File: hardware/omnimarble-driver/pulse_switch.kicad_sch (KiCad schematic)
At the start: 33 parts, among them J3 E-STOP-NC, J4 ARM-KEY, Q10 SFT040N150C3, Q11 SFT040N150C3, Q12 SFT040N150C3, U6 74LVC1G08, U7 UCC27524A, U8 UCC27524A

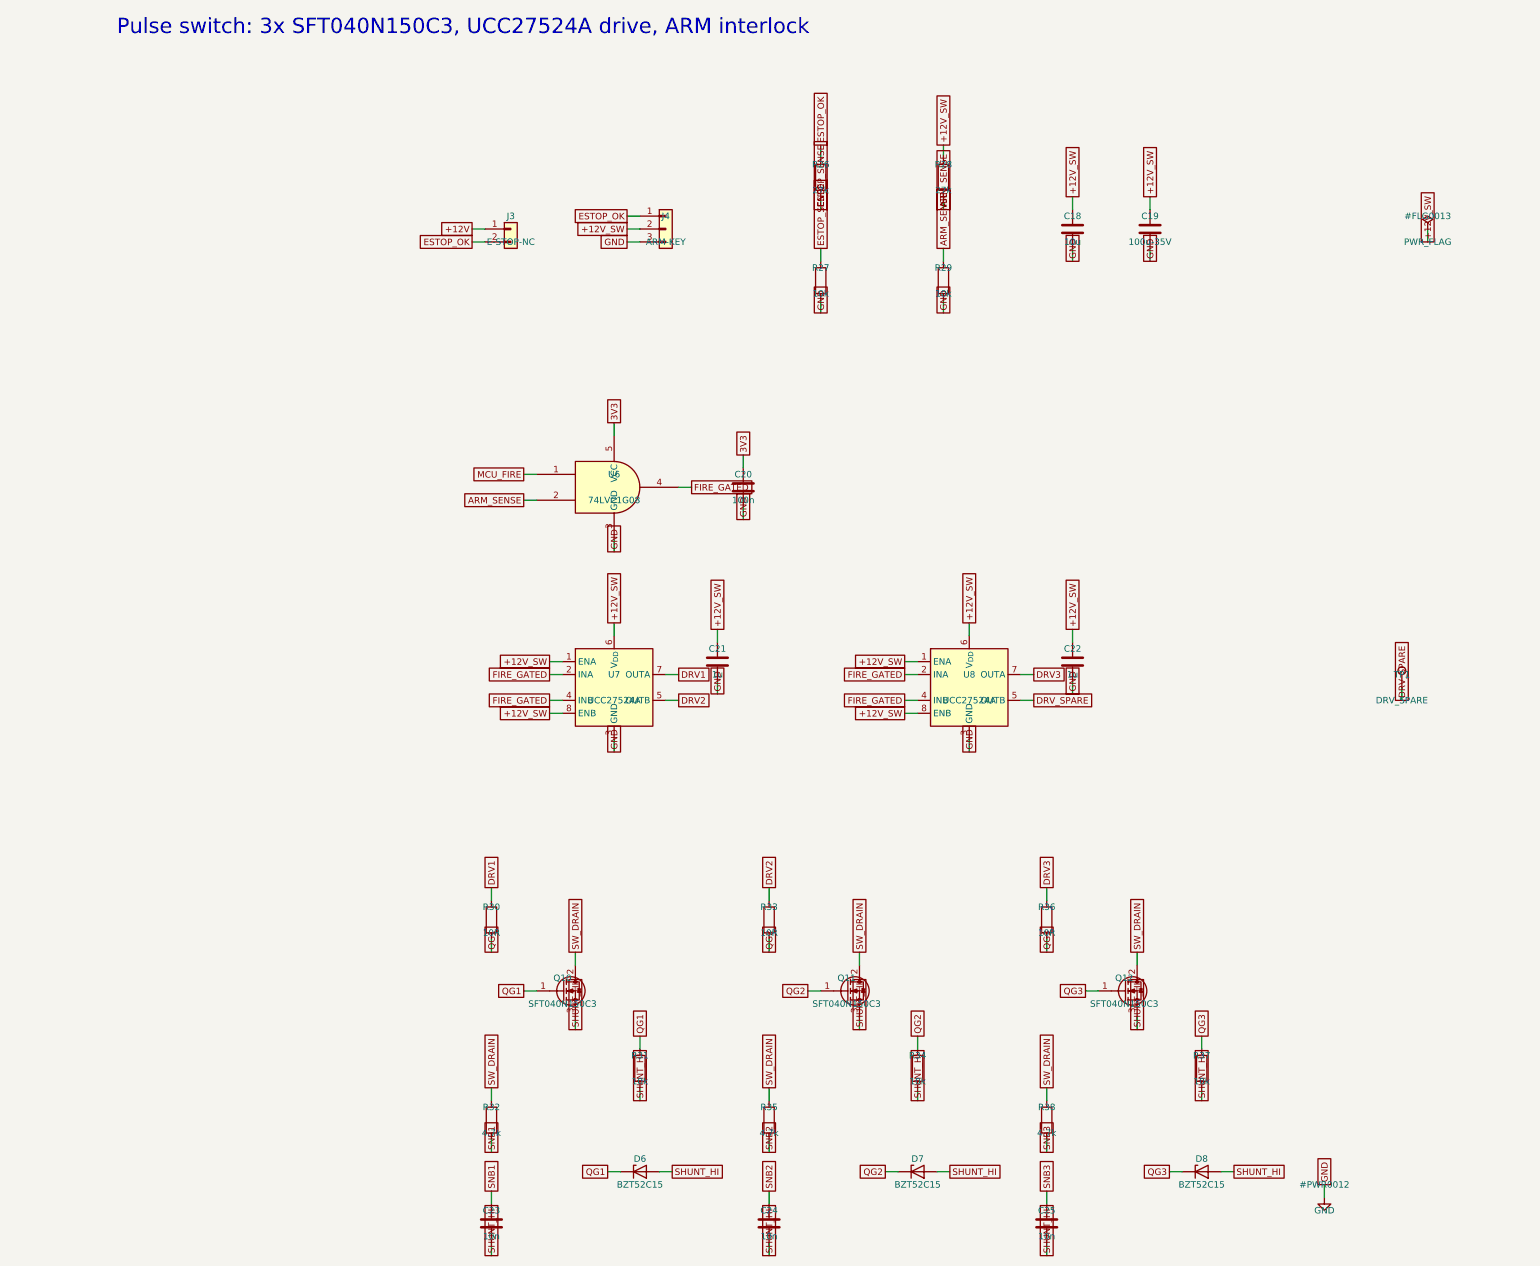
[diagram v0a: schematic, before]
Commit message: Address external design review: boost FB + OVP redesign, BOM freeze
Review findings accepted and fixed (each verified by machine check):

1. Boost feedback network was wrong (confirmed: as-drawn spanned
   54-68V with PWM inverted vs the comment). Redesigned: RT/RB/RJ =
   100k/10k/9.1k with the exact transfer function documented in the
   schematic and design-calcs.md. PWM=0 (MCU-dead state) commands
   55.0V; full PWM commands 18.7V (below the 24.5V converter floor).
   New calcs.py asserts both endpoints.
2. OVP tripped at 55.6V, not the claimed 63V (confirmed). Redesigned:
   CJ431 (+/-0.5%) + 100k/4.3k 1% -> 60.5V nominal, 59.1-62.0V across
   tolerances. Protection ladder asserted in calcs.py: 55V operating
   < 59.1V trip-min, 62.0V trip-max < 63V cap rating - 1V. Operating
   ceiling deliberately reduced 60->55V to keep the bands disjoint.
3. BOM/schematic controller split-brain: bom.csv was stale
   (pre-UC3843 swap); regenerated from parts.py. Both now UC3843B.
4. High-power placeholders now real orderable parts (LCSC-verified):
   47R/5W SQM cement C5807995, dump redesigned to 2x 100R/10W cement
   in series C216413 (no 20-25W part stocked on LCSC; 5.3s to <5V),
   50mR/3W 2512 C2994645, 63V/35V electrolytics C28241/C176666, 10uH
   Sunlord C79272, MINI fuses+Keystone 3568 holders, buzzer, Pico
   sockets/breakout headers. Single documented exception: the 6.8k/2W
   bleed (CRH2512J6K80E04Z) is marked ORDER-REVIEW because LCSC's
   search is uncrawlable - validate.py allowlists it visibly.
5. validate.py pulled forward from the fab phase: fails on unknown
   footprints, blank LCSC on machine-placed parts, missing Variant
   fields, and duplicate refs; generates per-variant gate-rail BOMs
   (bom_rail_emit/recv.csv). Caught two bad footprint names.
6. Paralleling constraints now on the schematic (same-lot FETs,
   symmetric copper, <25mm gate loops, driver return at shunt star).
7. Fail-safe defaults hardened: MCU_FIRE and FIRE_GATED get explicit
   pulldow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
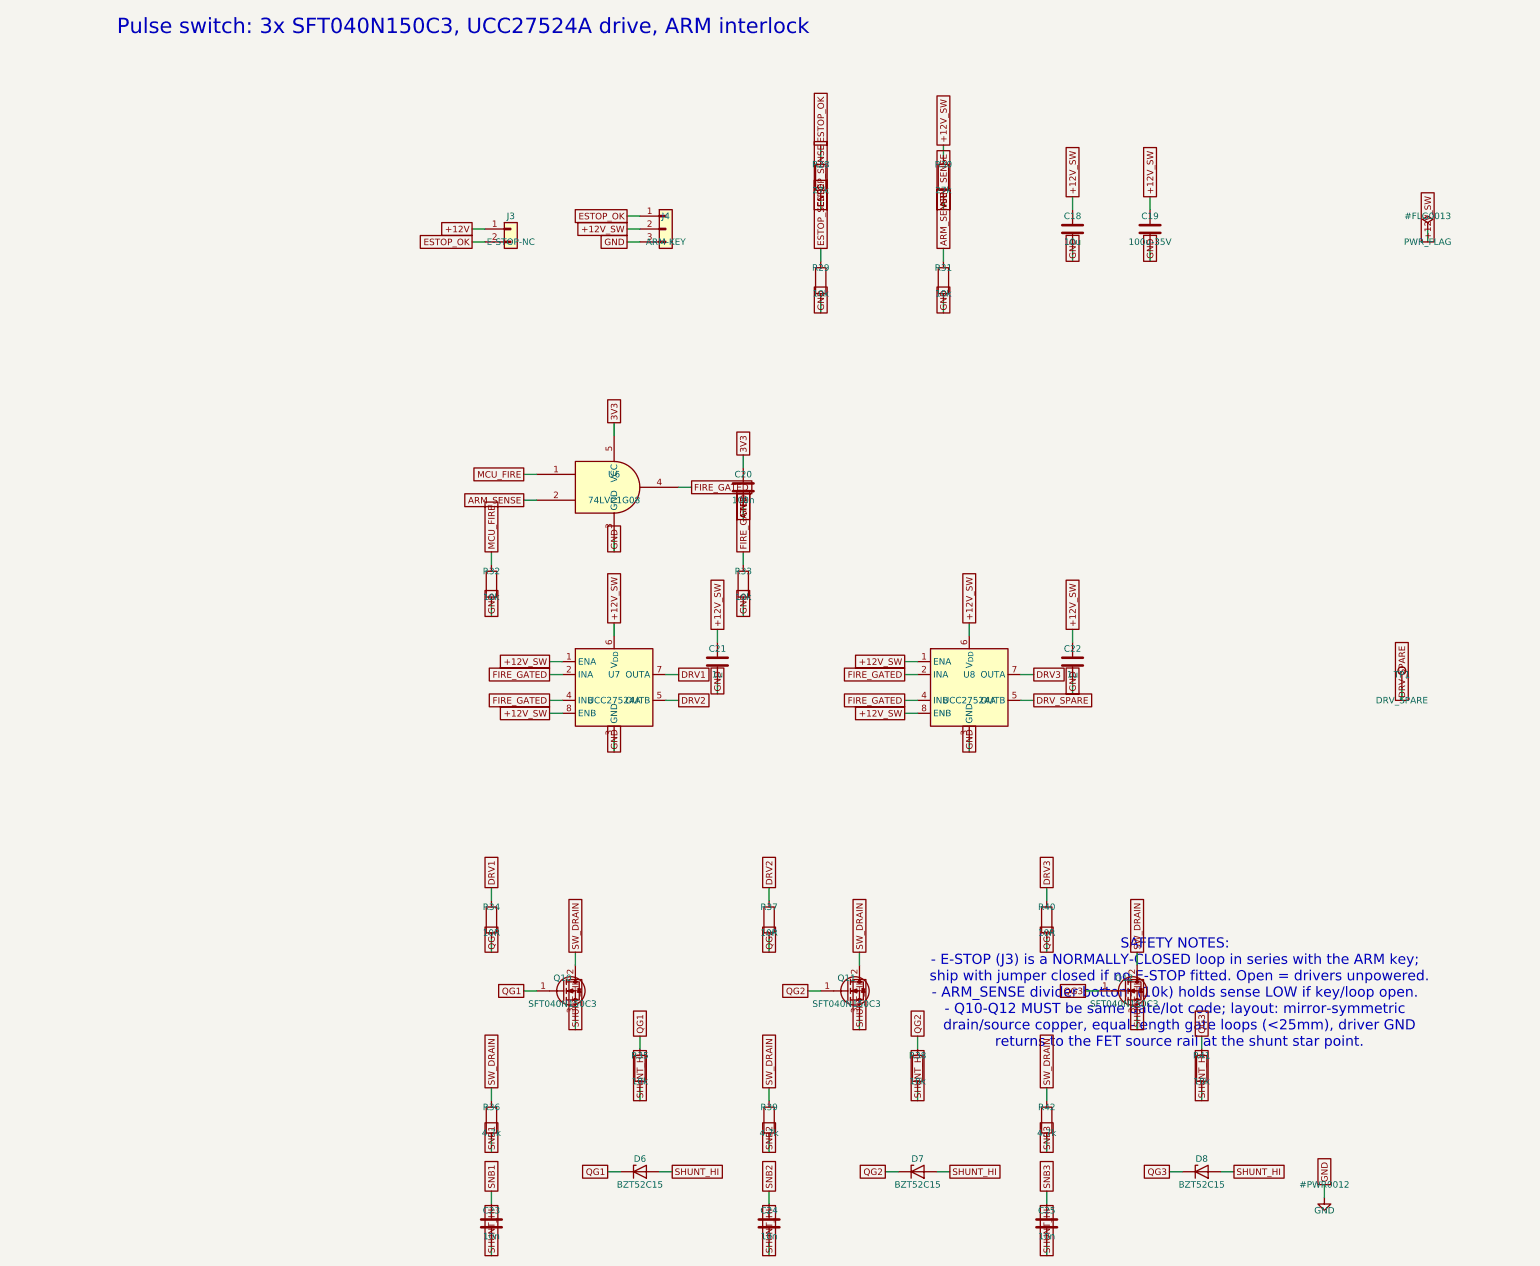
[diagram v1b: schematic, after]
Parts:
- removed R26: 27k, Resistor_SMD:R_0603_1608Metric, symbol Device:R
- removed R27: 10k, Resistor_SMD:R_0603_1608Metric, symbol Device:R
- added R39, R42: 4.7k, Resistor_SMD:R_2512_6332Metric, symbol Device:R
- added R40: 10R, Resistor_SMD:R_0603_1608Metric, symbol Device:R
- added R41: 10k, Resistor_SMD:R_0603_1608Metric, symbol Device:R
- C19: footprint Capacitor_SMD:CP_Elec_10x10.5 -> Capacitor_SMD:CP_Elec_6.3x7.7; LCSC (none) -> C176666
- C23, C24, C25: LCSC (none) -> C57112
- R28: LCSC (none) -> C22967
- R30: value 10R -> 27k; LCSC C22859 -> C22967
- R32, R35, R38: value 4.7k -> 10k; footprint Resistor_SMD:R_2512_6332Metric -> Resistor_SMD:R_0603_1608Metric; LCSC C23162 -> C25804
- R33: value 10R -> 10k; LCSC C22859 -> C25804
- R34, R37: value 10k -> 10R; LCSC C25804 -> C22859
- R36: value 10R -> 4.7k; footprint Resistor_SMD:R_0603_1608Metric -> Resistor_SMD:R_2512_6332Metric; LCSC C22859 -> C23162
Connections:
- net +12V_SW: now also R30.1; no longer R28.1
- net ARM_SENSE: now also R30.2, R31.1; no longer R28.2, R29.1
- net DRV1: now also R34.1; no longer R30.1
- net DRV2: now also R37.1; no longer R33.1
- net DRV3: now also R40.1; no longer R36.1
- net ESTOP_OK: now also R28.1
- net ESTOP_SENSE: now also R28.2, R29.1
- net FIRE_GATED: now also R33.1
- net GND: now also R31.2, R32.2, R33.2
- net MCU_FIRE: now also R32.1
- net QG1: now also R34.2, R35.1; no longer R30.2, R31.1
- net QG2: now also R37.2, R38.1; no longer R33.2, R34.1
- net QG3: now also R40.2, R41.1; no longer R36.2, R37.1
- net SHUNT_HI: now also R35.2, R38.2, R41.2; no longer R31.2, R34.2, R37.2
- net SNB1: now also R36.2; no longer R32.2
- net SNB2: now also R39.2; no longer R35.2
- net SNB3: now also R42.2; no longer R38.2
- net SW_DRAIN: now also R36.1, R39.1, R42.1; no longer R32.1, R35.1, R38.1
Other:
- note added: "SAFETY NOTES: - E-STOP (J3) is a NORMALLY-CLOSED loop in series with the ARM key; ship with jumper closed if no E-STOP fitted. Open = drivers unpowered. - ARM_SENSE divider bottom (10k) holds sense LOW if key/loop open. - Q10-Q12 MUST be same date/lot code; layout: mirror-symmetric drain/source copper, equal-length gate loops (<25mm), driver GND returns to the FET source rail at the shunt star po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"

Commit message: Datasheet-exact footprints, placement engine, scripted PCB router WIP
- gen_footprints.py: TOLL-8, D2PAK (cathode-tab corrected), 5930 shunt,
  9.5mm barrier, HF3FF relay land patterns; drop _DRAFT footprints
- placement.py: 220x150 board plan, pulse zone polygons derived from
  package pad windows, shelf-packed clusters, Kelvin/manual tracks
- gen_pcb.py: netlist->board generator with zone builder, via stitching,
  pad-in-zone assertions, straggler/GND-drop/escape pre-routes and a
  negotiated-congestion (PathFinder-lite) signal router + greedy cleanup
- debug_route.py/debug_map.py/debug_j7.py: router diagnostics

Co-Authored-By: Claude Fable 5 <noreply@anthropic.com>
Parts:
- Q10, Q11, Q12: footprint omnimarble:TOLL-8_DRAFT -> omnimarble:TOLL-8

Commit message: Driver PCB: fix schematic parity + correct review overclaims
Addresses external review pushback on the "DRC-clean/fab-ready" framing.

- Schematic parity now 0 (was 6): footprint DNP synced for C92-94; TP1/
  NT1/NT2 excluded from BOM in schematic (test point + Kelvin net-ties).
  kicad_sch.add_symbol gains in_bom kwarg so this can't regress.
- REVIEW_HANDOFF.md rev 2: drops "DRC-clean copper" overclaim. States
  honestly this is an iteration checkpoint, not fab-ready: 59 real
  clearance errors (near-shorts to 0.010mm on FIRE_GATED/gate/BOOST_EN_N/
  ESTOP nets), 118 unconnected incl 34 safety/control/analog. Clarifies
  board is byte-identical (sha256 ed02f3b) across e64fb78/bb3ea38/ae83ebe.
- Review dashboard: verdict banner amber "iteration checkpoint - not
  fab-ready"; clearance + unconnected reclassed as blockers; parity row
  added; agreed next gate (0 unconn / 0 clearance / 0 parity + manual
  power-loop review) replaces the open-questions block.
- ERC still 0.

Co-Authored-By: Claude Fable 5 <noreply@anthropic.com>
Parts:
- TP1: now left out of the parts list
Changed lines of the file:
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@@
 		(unit 1)
 		(exclude_from_sim no)
-		(in_bom yes)
+		(in_bom no)
 		(on_board yes)
 		(dnp no)

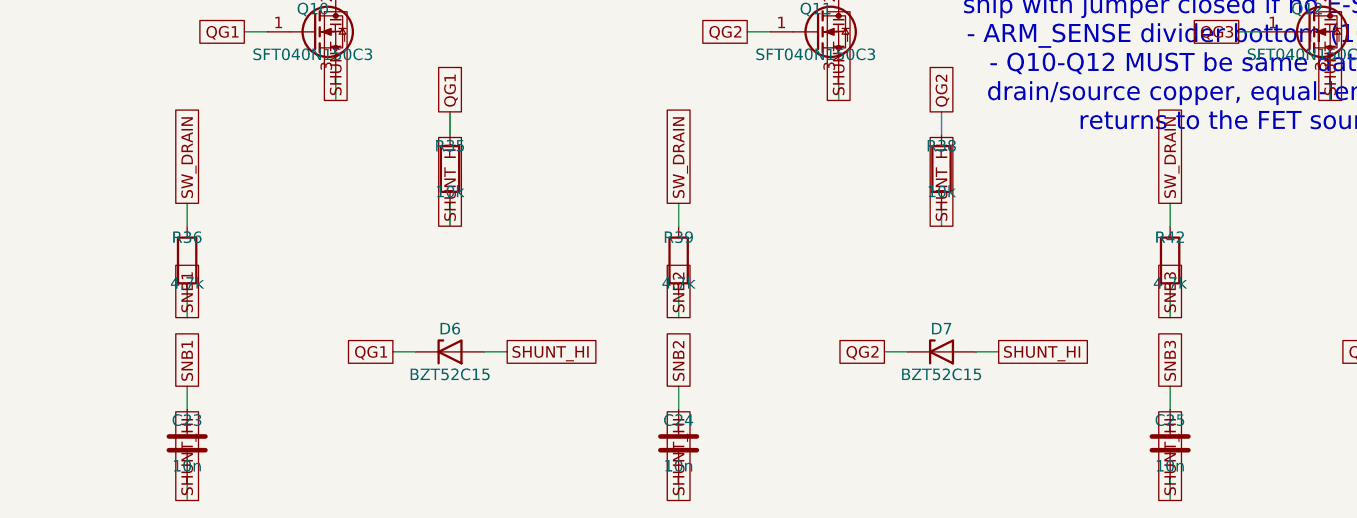
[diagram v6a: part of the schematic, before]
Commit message: Driver PCB: resolve both safety blockers + should-fixes, re-route, DRC-clean
Two datasheet-level blockers (invisible to netlist checks) + the should-fixes
from two review rounds, then a full DeepPCB re-route on the corrected netlist.

Blockers:
- U5 shunt ref: CJ431/C3113 (pinout 1=REF,2=K,3=A) did NOT match the TL431DBZ
  footprint -> OVP dead. Now TL431BIDBZR/C41283 (+/-0.5%, 1=K,2=REF,3=A). Kept
  +/-0.5% grade (the 1% A-grade would blow the 62.0V OVP ceiling).
- Relay HF3FF footprint had NO/NC transposed (datasheet bottom-view copied
  without mirroring) -> dump/charge logic inverted. Swapped pads 12<->14 +
  corrected silk. VERIFY WITH OHMMETER at bring-up (COM-NC @rest) -- parity is
  green by construction, DRC cannot see this.

Should-fixes: D90 SMBJ33A->SMBJ26CA (bidirectional, clamps below AP63205);
snubber 4.7k->4.7Ohm; R7 0.05->0.15Ohm (boost ilim); R25 10k->47k (0.28W->0.06W
LED series); BZ1 polarity swap. 78L12->DPAK deferred (reflows the placement
band; documented, fan-cool for bench per user).

Routing: full DeepPCB re-route from the corrected DSN. dsn_fixup now injects a
B.Cu keepout over the FET-strip corridor so the router can't pack signals where
the SHUNT_HI bus lives (rev-40 dropped the locked bus). import-clean re-authors
the SHUNT_HI B.Cu bus deterministically. Post-import repairs: re-authored the
RS1->NT1 Kelvin tie (DeepPCB routed SHUNT_HI on F.Cu shorting ISNS_P), joined a
MCU_FIRE via gap, bulged GATE6 off a 3V3 via, island-removal + a stitch via to
unify the fragmented F.Cu SHUNT_HI pour.

DRC 0 electrical / 0 unconnected; validate.py --production, validate_widths,
check_netlist, calcs all PASS.

Co-Authored-By: Claude Opus 4.8 <noreply@anthropic.com>
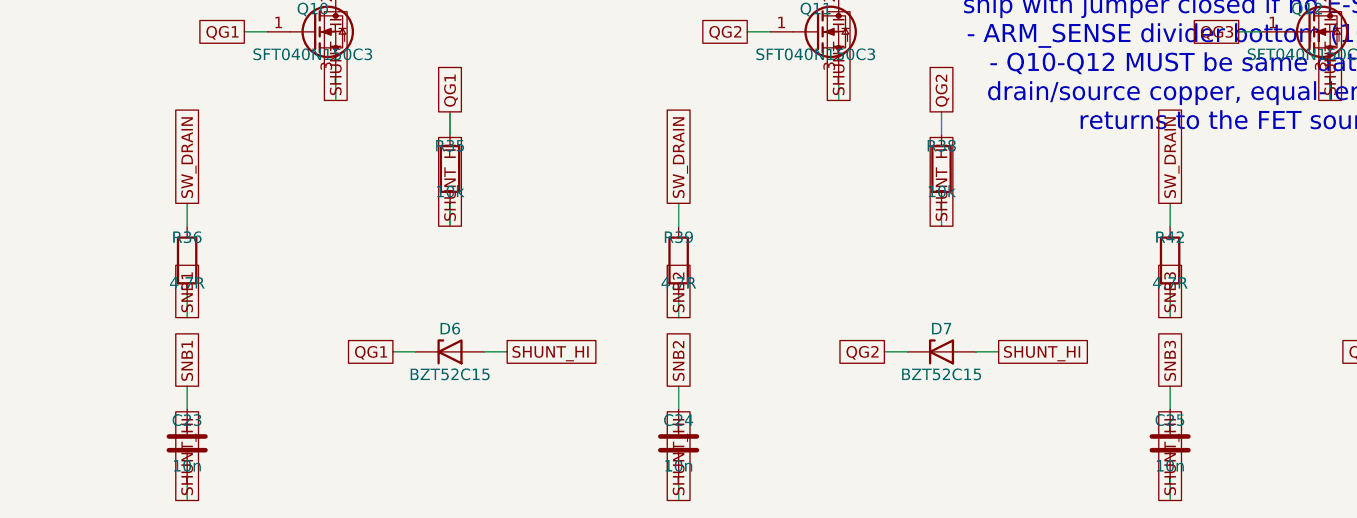
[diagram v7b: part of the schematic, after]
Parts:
- R36, R39, R42: value 4.7k -> 4.7R; LCSC C23162 -> C146897

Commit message: Snapshot driver's final validated state before parking as vNext
Fold the last regeneration into the repo so the source is internally consistent
with the already-committed board/BOM (the Q90 diode->MOSFET fix + JLC cart
substitutions previously landed only in the root schematic + board):
- 7 driver schematic sub-sheets, regenerated to carry the final part numbers.
- fab/jlc/ORDER_NOTES.md — final BOM (J2/J5 C707836, R21/R22 C5110275, etc.).
- omnimarble-driver-5-rev-39.ses — the routing session import-clean rebuilds the
  board from; committing it keeps the routed board reproducible while parked.

Timestamp-only gerber/zip churn and scratch (.ses iterations, drc/erc reports,
logs) were left out. Driver stays vNext/on-hold per V0_BENCH_RIG.md.

Co-Authored-By: Claude Opus 4.8 <noreply@anthropic.com>
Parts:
- R36, R39, R42: LCSC C146897 -> C25489
